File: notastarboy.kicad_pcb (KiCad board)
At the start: 2 copper layers, 53.5 x 64.5 mm, 7 parts, among them J1 Conn_01x04_Pin, J2 Conn_01x08_Pin, SW1 SW_Push, SW2 SW_Push, U1 XIAO-ESP32-C3-SMD, U2 DHT11

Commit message: Made the pcb, designed it to be a bit cool but ROUTING is incomplete rn
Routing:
- net GND: track 0.00 -> 148.0 mm
- net +3.3V: track 0.00 -> 123.4 mm
- net /GPIO2: track 0.00 -> 105.2 mm
- net /DHT11 DATA: track 0.00 -> 41.1 mm
- net /GPIO3: track 0.00 -> 40.1 mm
- net /SCL: track 0.00 -> 36.7 mm
- net /SDA: track 0.00 -> 35.4 mm
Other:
- board size 53.5 x 64.5 mm -> 54.2 x 64.5 mm

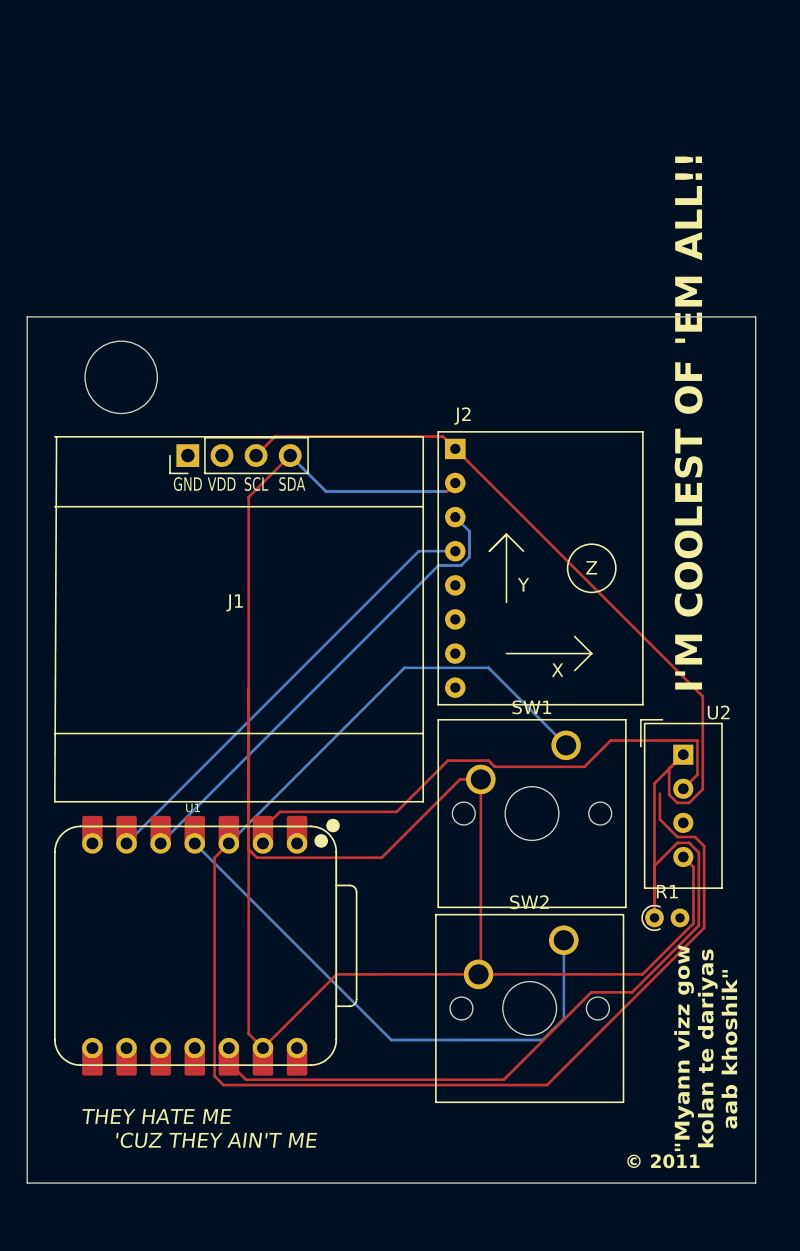
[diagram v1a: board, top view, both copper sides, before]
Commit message: routing complete and apprantly pcb works now
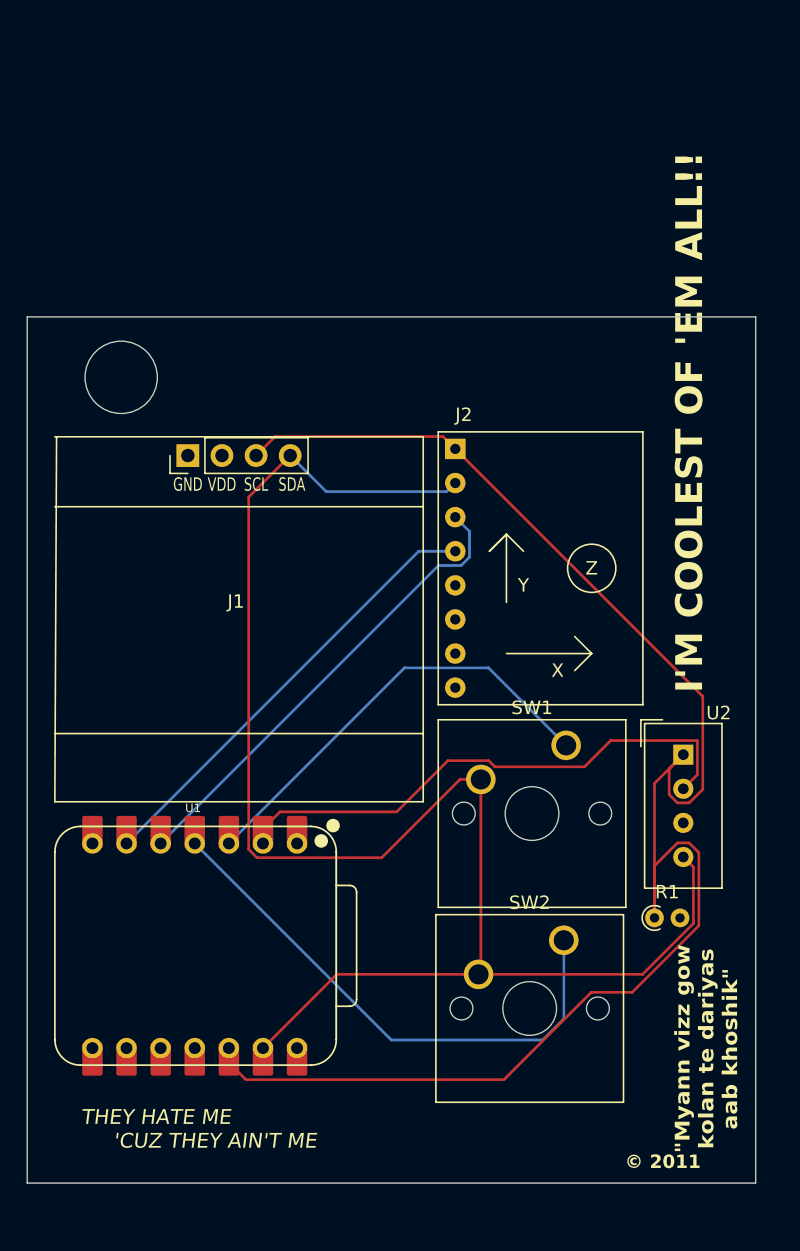
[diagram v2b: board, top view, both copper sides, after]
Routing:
- net /GPIO2: track 105.2 -> 33.8 mm
- net GND: track 148.0 -> 120.0 mm

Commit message: I remade the schematic cuz i messed up net labels in the first one
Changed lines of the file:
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@@
 		)
 		(fp_text user "SCL"
-			(at 1.27 2.159 0)
+			(at 1.27 2.175 0)
 			(layer "F.SilkS")
 			(effects

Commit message: cleaned up the schematic even more and hopefully its the final version
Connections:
- J1 pad 1: unconnected-(J1-Pin_1-Pad1) -> /SDA
- J1 pad 2: unconnected-(J1-Pin_2-Pad2) -> /SCL
- R1 pad 2: unconnected-(R1-Pad2) -> /DHT11 DATA
- U1 pad 2: /DHT11 DATA -> /DHT11_DATA
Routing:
- net +3.3V: track 123.4 -> 0.00 mm
- net GND: track 120.0 -> 0.00 mm
- net /DHT11 DATA: track 41.1 -> 0.00 mm
- net /GPIO3: track 40.1 -> 0.00 mm
- net /SCL: track 36.7 -> 0.00 mm
- net /SDA: track 35.4 -> 0.00 mm
- net /GPIO2: track 33.8 -> 0.00 mm

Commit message: FINALLY COMPLETED THE PCB ROUTING AS WELL!!!!
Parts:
- moved U1 2.84 mm to (93.8, 101.8), turned to 180 degrees
- moved SW2 2.50 mm to (118.5, 103.9)
- moved SW1 0.52 mm to (118.5, 87.4)
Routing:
- net GND: track 0.00 -> 164.6 mm
- net +3.3V: track 0.00 -> 111.6 mm
- net /SDA: track 0.00 -> 89.4 mm
- net /SCL: track 0.00 -> 74.4 mm
- net /GPIO2: track 0.00 -> 36.4 mm
- net /GPIO3: track 0.00 -> 28.5 mm
- net /DHT11 DATA: track 0.00 -> 10.6 mm

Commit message: final render and final pcb
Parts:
- added G***: LOGO, graphics:omg, B.Cu at (108.0, 93.0)
- moved R1 5.77 mm to (129.6, 103.5)
- moved U2 2.93 mm to (130.0, 88.9)
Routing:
- net +3.3V: track 111.6 -> 118.0 mm
- net /DHT11 DATA: track 10.6 -> 16.8 mm
- net GND: track 164.6 -> 167.9 mm
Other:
- board size 54.2 x 64.5 mm -> 55.5 x 67.5 mm

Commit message: all files ready
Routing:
- net /DHT11 DATA: track 16.8 -> 12.7 mm
- net +3.3V: track 118.0 -> 116.5 mm
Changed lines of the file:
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@@
 			(sketchdnponfab yes)
 			(crossoutdnponfab yes)
-			(subtractmaskfromsilk no)
+			(subtractmaskfromsilk yes)
 			(outputformat 1)
 			(mirror no)
-			(drillshape 1)
+			(drillshape 0)
 			(scaleselection 1)
-			(outputdirectory "")
+			(outputdirectory "gerber/")
 		)
 	)
@@
 	)
 	(segment
-		(start 128.55 102.45)
-		(end 129.6 103.5)
-		(width 0.2)
-		(layer "F.Cu")
-		(net "+3.3V")
-	)
-	(segment
 		(start 130 88.88)
 		(end 131.085786 89.965786)
@@
 	)
 	(segment
-		(start 127.36 87.5)
-		(end 127.36 87.6)
-		(width 0.2)
-		(layer "B.Cu")
-		(net "+3.3V")
-	)
-	(segment
 		(start 111.442 70.349895)
 		(end 111.442 69.470105)
@@
 	)
 	(segment
-		(start 127.32 95.18)
-		(end 127.36 95.22)
-		(width 0.2)
-		(layer "F.Cu")
-		(net "GND")
-	)
-	(segment
 		(start 88.7385 93.376)
 		(end 88.7385 104.993105)
@@
 	)
 	(segment
-		(start 128.41 100.41)
-		(end 131.5 103.5)
-		(width 0.2)
-		(layer "B.Cu")
-		(net "/DHT11 DATA")
-	)
-	(segment
-		(start 127.36 90.14)
-		(end 128.41 91.19)
-		(width 0.2)
-		(layer "B.Cu")
-		(net "/DHT11 DATA")
-	)
-	(segment
-		(start 128.41 91.19)
-		(end 128.41 100.41)
-		(width 0.2)
-		(layer "B.Cu")
-		(net "/DHT11 DATA")
-	)
-	(segment
-		(start 128.41 91.19)
-		(end 128.64 91.42)
+		(start 131.5 92.92)
+		(end 130 91.42)
 		(width 0.2)
 		(layer "B.Cu")
@@
 	)
 	(segment
-		(start 128.64 91.42)
-		(end 130 91.42)
+		(start 131.5 103.5)
+		(end 131.5 92.92)
 		(width 0.2)
 		(layer "B.Cu")
